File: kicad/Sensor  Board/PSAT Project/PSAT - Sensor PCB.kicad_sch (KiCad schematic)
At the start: 16 parts, among them J1 MCU Conn_01x04, J2 Conn_01x02, J3 Conn_01x03, J4 Conn_01x03, J5 Conn_01x01, U1 MPU-6000, U2 BME280

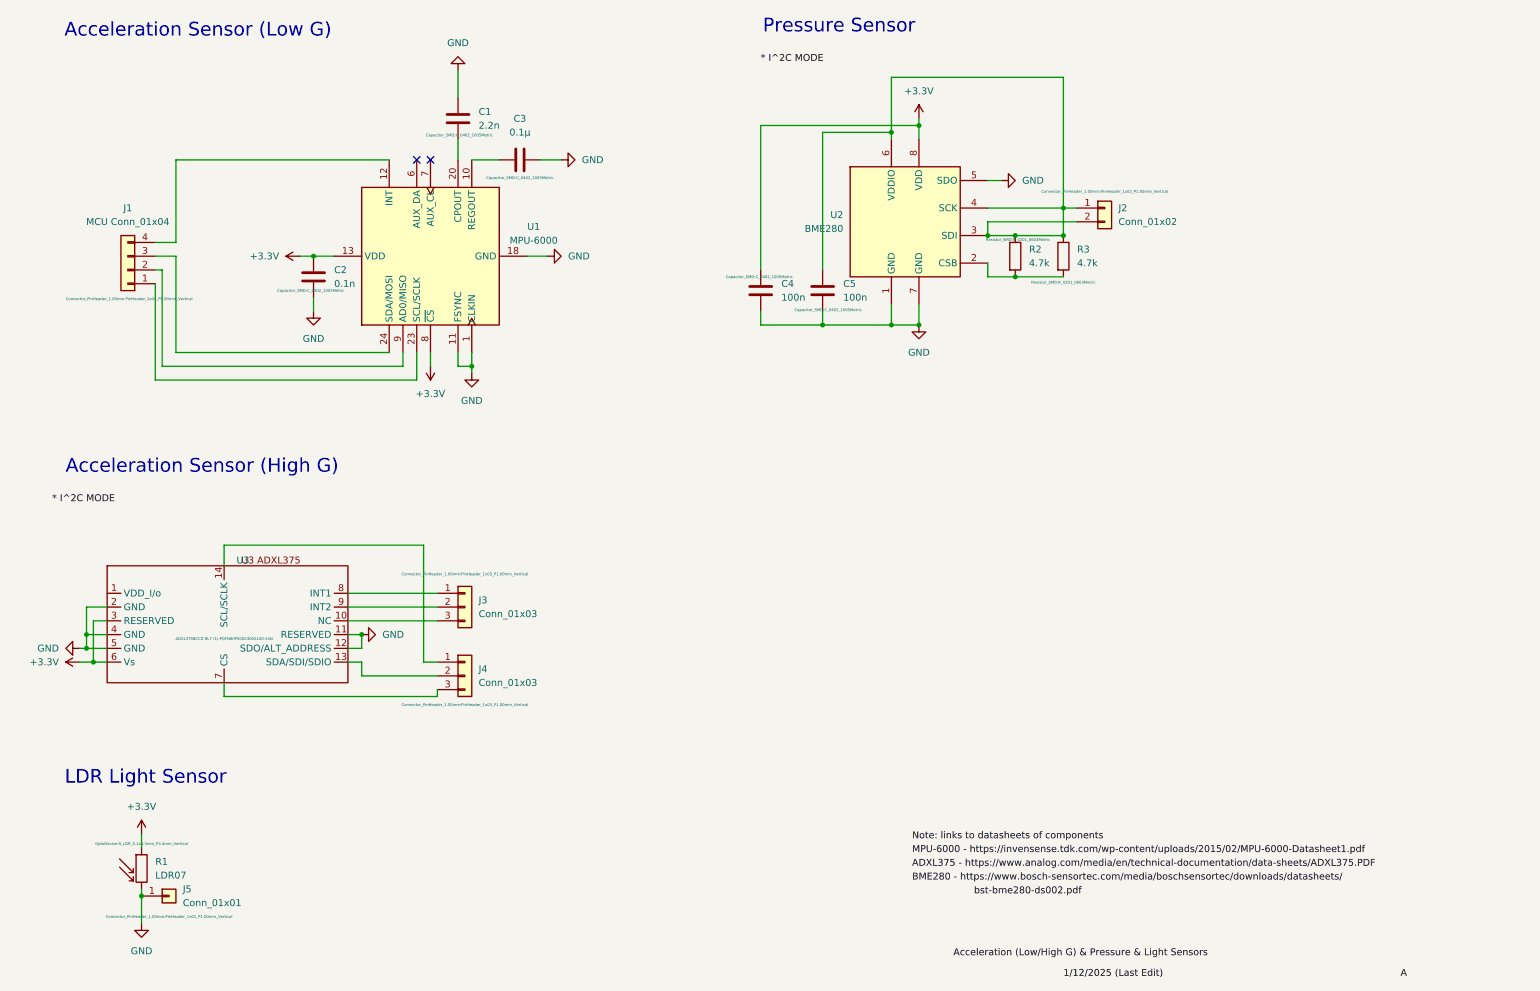
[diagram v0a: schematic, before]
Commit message: Updated Sensor board: Pin corrections + added footprint
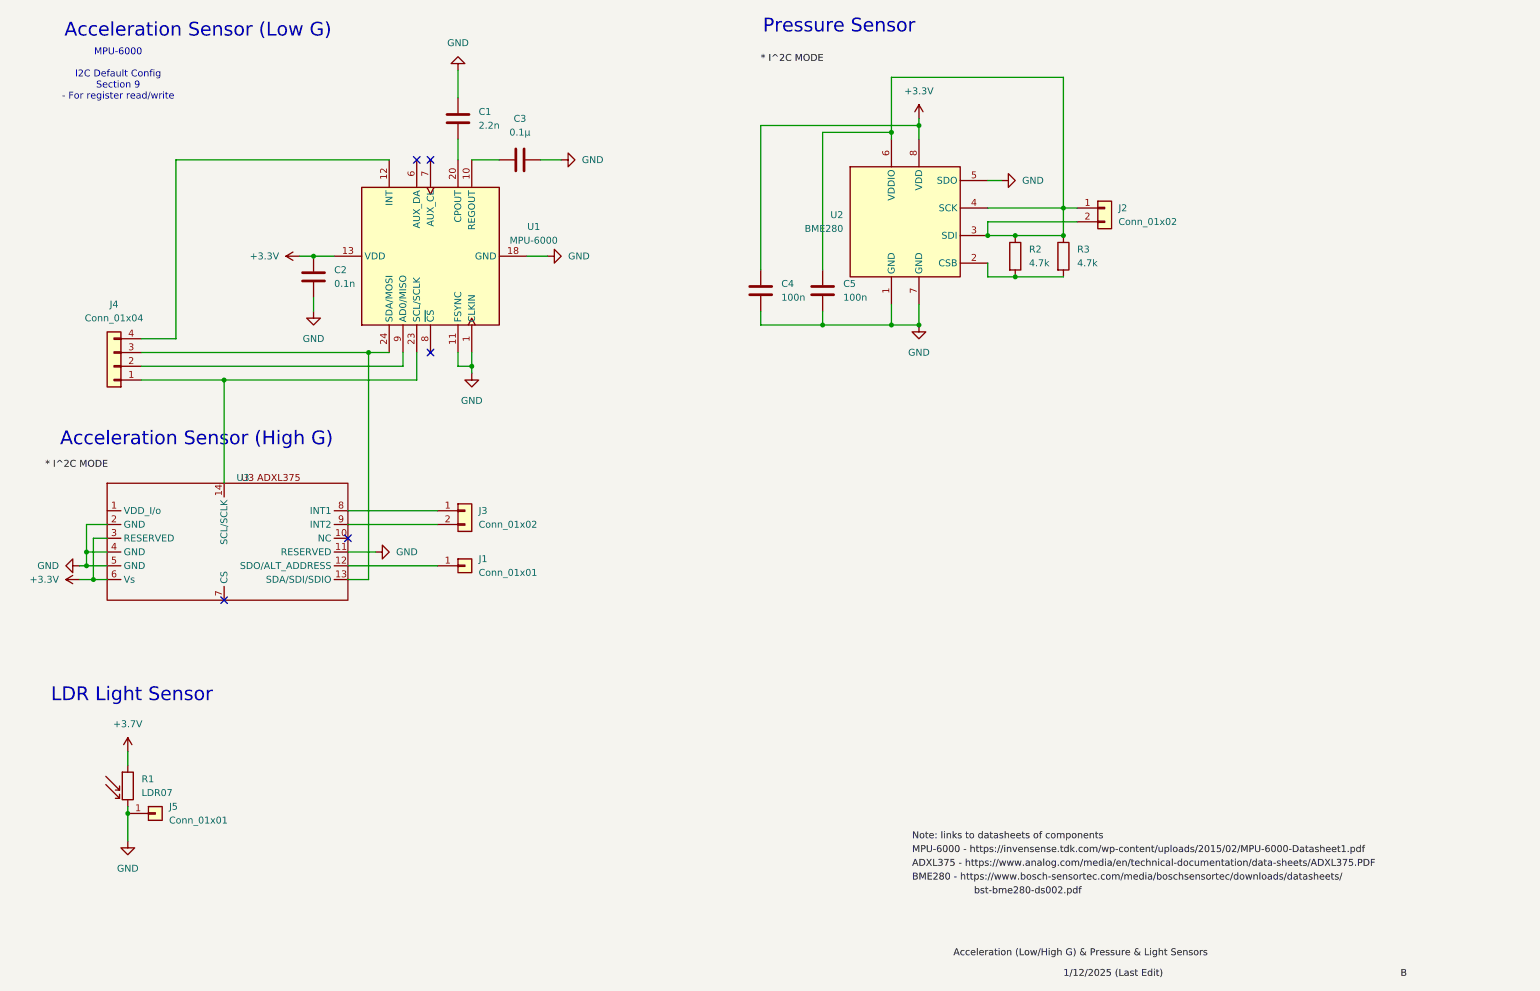
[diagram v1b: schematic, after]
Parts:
- removed J1: MCU Conn_01x04, Connector_PinHeader_1.00mm:PinHeader_1x04_P1.00mm_Vertical, symbol Connector_Generic:Conn_01x04
- removed J3, J4: Conn_01x03, Connector_PinHeader_1.00mm:PinHeader_1x03_P1.00mm_Vertical, symbol Connector_Generic:Conn_01x03
- added J1: Conn_01x01, symbol Connector_Generic:Conn_01x01
- added J3: Conn_01x02, symbol Connector_Generic:Conn_01x02
- added J4: Conn_01x04, symbol Connector_Generic:Conn_01x04
- C1, C2, C3, C4, C5: footprint Capacitor_SMD:C_0402_1005Metric -> Capacitor_SMD:C_0805_2012Metric_Pad1.18x1.45mm_HandSolder
- J2: footprint Connector_PinHeader_1.00mm:PinHeader_1x02_P1.00mm_Vertical -> (none)
- J5: footprint Connector_PinHeader_1.00mm:PinHeader_1x01_P1.00mm_Vertical -> (none)
- R1: footprint OptoDevice:R_LDR_5.1x4.3mm_P3.4mm_Vertical -> OptoDevice:R_LDR_D13.8mm_P9.0mm_Vertical
- R2, R3: footprint Resistor_SMD:R_0201_0603Metric -> Resistor_SMD:R_0805_2012Metric_Pad1.20x1.40mm_HandSolder
- U1: footprint Sensor_Motion:InvenSense_QFN-24_4x4mm_P0.5mm -> (none)
- U2: footprint Package_LGA:Bosch_LGA-8_2.5x2.5mm_P0.65mm_ClockwisePinNumbering -> (none)
- U3: footprint ADXL375BCCZ-RL7 (1):PQFN80P500X300X100-14N -> ADXL375:0805 CAP
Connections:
- net +3.3V: no longer R1.1, U1.8 (~{CS})
- net GND: no longer U3.12 (SDO/ALT_ADDRESS)
- net at U3.13 (SDA/SDI/SDIO): now also U1.24 (SDA/MOSI), J4.3 (Pin_3)
- net at U3.14 (SCL/SCLK): now also U1.23 (SCL/SCLK), J4.1 (Pin_1)
- net at U3.8 (INT1): now also J3.1 (Pin_1)
- net at U3.9 (INT2): now also J3.2 (Pin_2)
- net at U1.12 (INT): now also J4.4 (Pin_4)
- net at U1.9 (AD0/MISO): now also J4.2 (Pin_2)
- new net: J1.1 (Pin_1), U3.12 (SDO/ALT_ADDRESS)
- new net +3.7V: R1.1
- no-connect marks 2 -> 5
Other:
- note added: "MPU-6000 I2C Default Config Section 9 - For register read/write"
- moved on the sheet: J5, R1, U3

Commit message: Modified sensor board, added an enable section for the pressure sensor and cleaned up the schematic with global labels
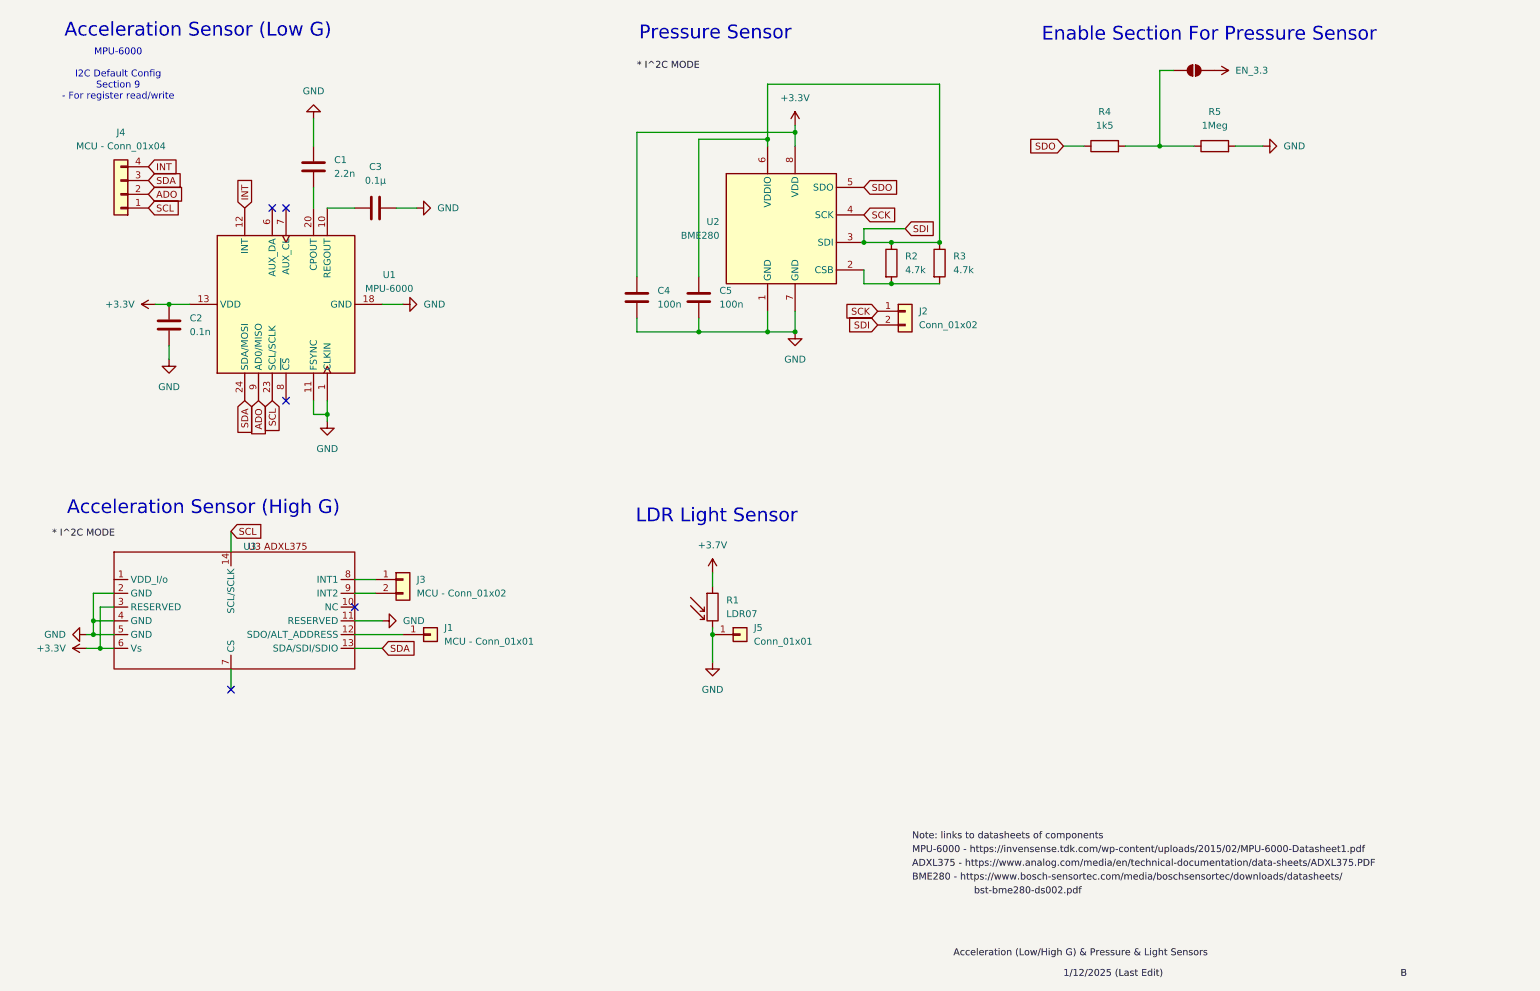
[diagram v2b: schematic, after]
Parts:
- added JP1: EN_5, Jumper:SolderJumper-2_P1.3mm_Open_Pad1.0x1.5mm, symbol Jumper:SolderJumper_2_Open
- added R4: 1k5, Resistor_SMD:R_0402_1005Metric, symbol Device:R
- added R5: 1Meg, Resistor_SMD:R_0402_1005Metric, symbol Device:R
- J1: value Conn_01x01 -> MCU - Conn_01x01
- J3: value Conn_01x02 -> MCU - Conn_01x02
- J4: value Conn_01x04 -> MCU - Conn_01x04
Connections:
- net GND: now also R5.2; no longer U2.5 (SDO)
- net SDA: now reaches J4.3 (Pin_3), U1.24 (SDA/MOSI), U3.13 (SDA/SDI/SDIO)
- net SCL: now reaches J4.1 (Pin_1), U1.23 (SCL/SCLK), U3.14 (SCL/SCLK)
- net SDI: now reaches C5.1, J2.2 (Pin_2), R2.1, R3.1, U2.3 (SDI), U2.6 (VDDIO)
- net SDI: no longer J2.1 (Pin_1), U2.4 (SCK)
- net ADO: now reaches J4.2 (Pin_2), U1.9 (AD0/MISO)
- net INT: now reaches J4.4 (Pin_4), U1.12 (INT)
- new net: JP1.2 (B), R4.2, R5.1
- new net EN_3.3: JP1.1 (A)
- new net SCK: J2.1 (Pin_1), U2.4 (SCK)
- new net SDO: R4.1, U2.5 (SDO)
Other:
- note added: "Enable Section For Pressure Sensor"
- moved on the sheet: C1, C2, C3, C4, C5, J1, J2, J3, J4, J5, R1, R2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
